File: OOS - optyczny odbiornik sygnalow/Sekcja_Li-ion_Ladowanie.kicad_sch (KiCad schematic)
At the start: 45 parts, among them J1 Conn_01x02_Pin, Q1 SI2301CDS-T1-GE3, Q2 AOSS32334C, Q3 AOSS32334C, U4 MCP73831T-2ATI/OT, U5 AP9101CAK6-ANTRG1, U6 AP2126K-ADJTRG1

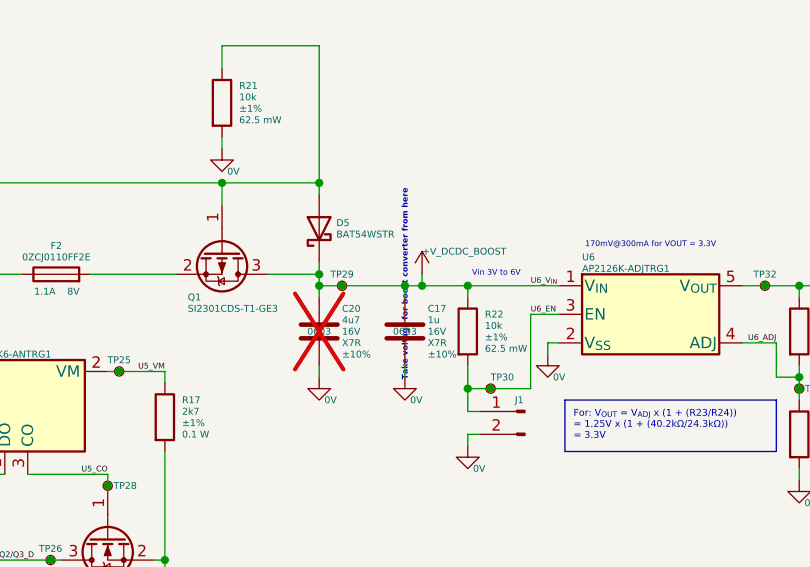
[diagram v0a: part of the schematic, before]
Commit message: Clean schematic, what left is to add resistors for pull down on usb page and rotary switch on analog page
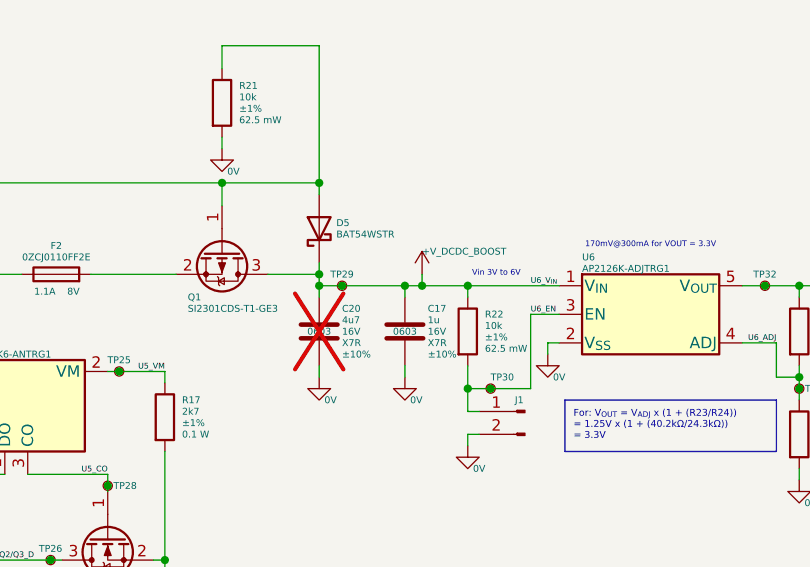
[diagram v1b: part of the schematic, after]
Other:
- note removed: "Take voltage for boost converter from here"
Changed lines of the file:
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@@
-		)
-	)
-	(text "Take voltage for boost converter from here"
-		(exclude_from_sim no)
-		(at 193.675 77.47 90)
-		(effects
-			(font
-				(size 0.635 0.635)
-				(thickness 0.127)
-				(bold yes)
-				(color 255 0 0 1)
-			)
 		)
 	)
